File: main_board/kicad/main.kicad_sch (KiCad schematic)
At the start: 1 part

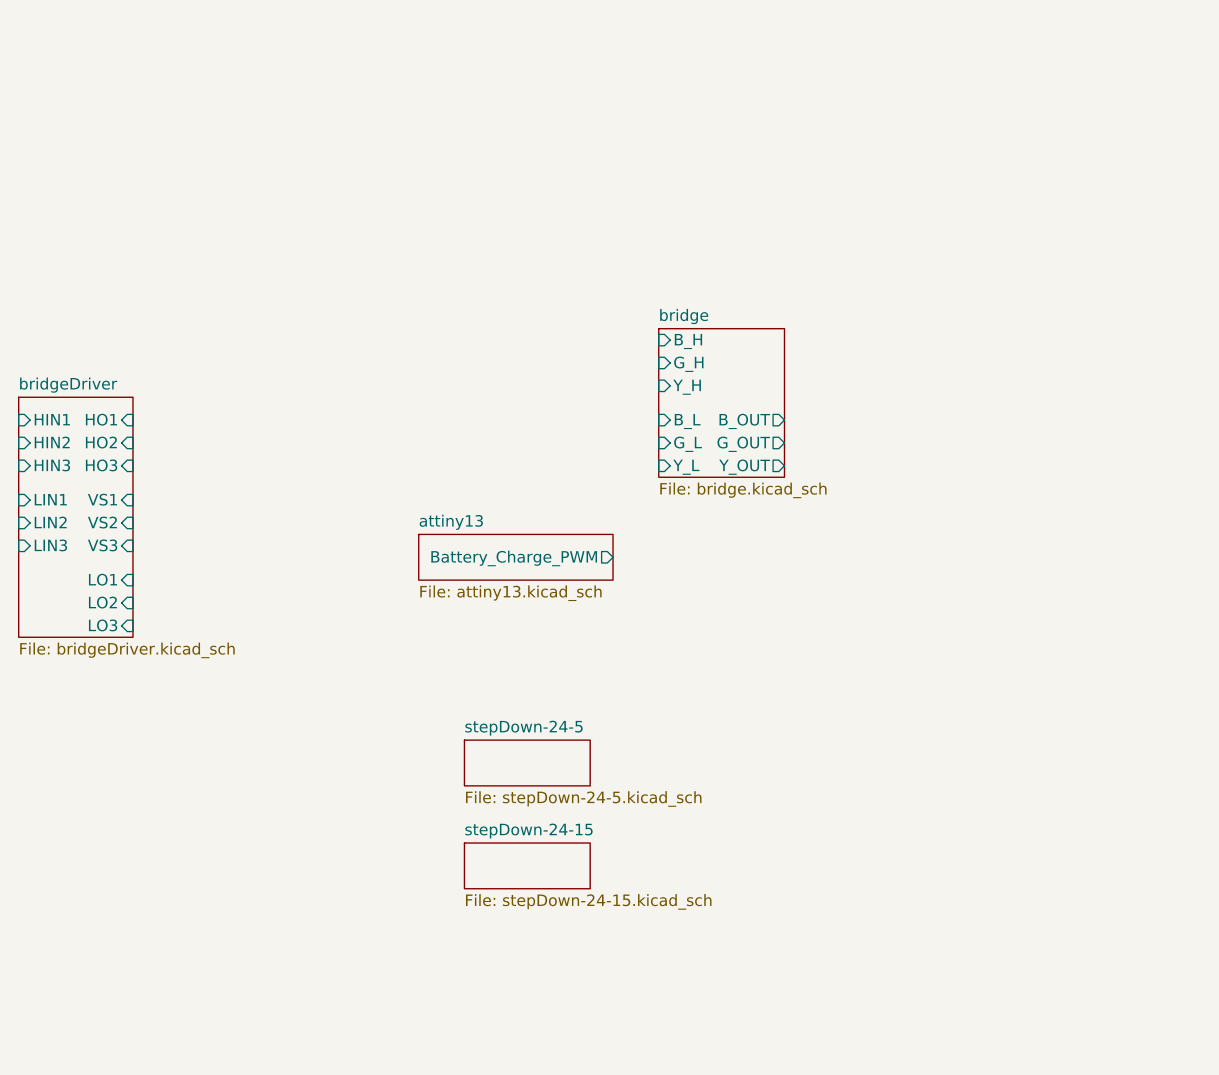
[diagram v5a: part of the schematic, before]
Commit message: added communication logic
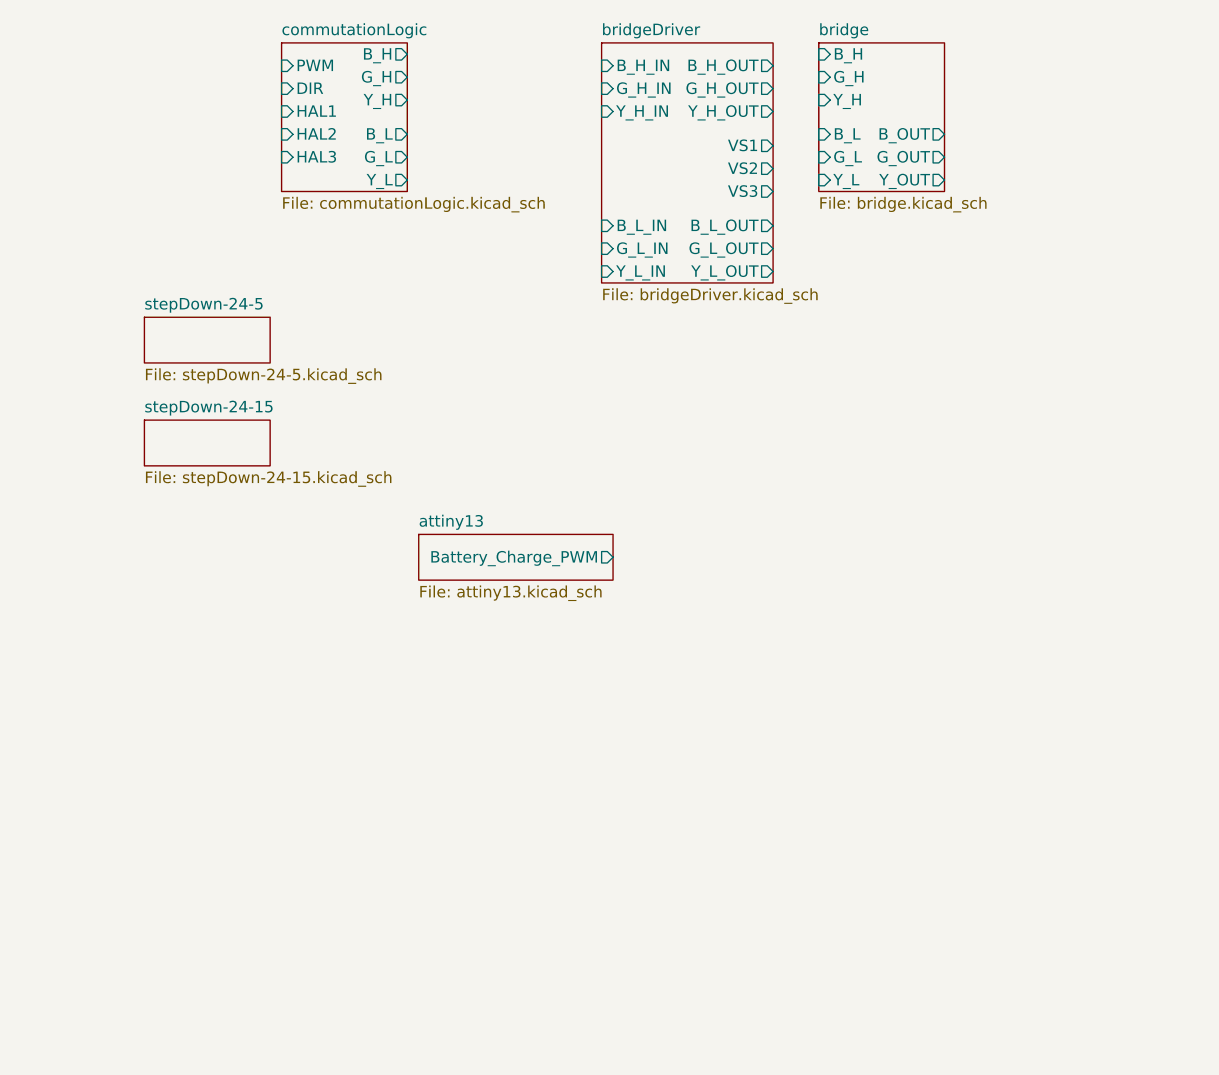
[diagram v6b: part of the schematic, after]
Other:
- added sheet commutationLogic (commutationLogic.kicad_sch)
- sheet bridgeDriver ports: added B_H_IN, B_H_OUT, B_L_IN, B_L_OUT, G_H_IN, G_H_OUT, G_L_IN, G_L_OUT, Y_H_IN, Y_H_OUT, Y_L_IN, Y_L_OUT; removed HIN1, HIN2, HIN3, HO1, HO2, HO3, LIN1, LIN2, LIN3, LO1, LO2, LO3
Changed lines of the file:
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@@
     )
   )
-  (sheet (at 180.34 138.43) (size 13.97 16.51) (fields_autoplaced)
+  (sheet (at 198.12 106.68) (size 13.97 16.51) (fields_autoplaced)
     (stroke (width 0.1524) (type solid))
     (fill (color 0 0 0 0.0000))
-    (property "Sheetname" "bridge" (at 180.34 137.7184 0)
+    (property "Sheetname" "bridge" (at 198.12 105.9684 0)
       (effects (font (size 1.27 1.27)) (justify left bottom))
     )
-    (property "Sheetfile" "bridge.kicad_sch" (at 180.34 155.5246 0)
+    (property "Sheetfile" "bridge.kicad_sch" (at 198.12 123.7746 0)
       (effects (font (size 1.27 1.27)) (justify left top))
     )
-    (pin "G_H" input (at 180.34 142.24 180)
+    (pin "G_H" input (at 198.12 110.49 180)
       (effects (font (size 1.27 1.27)) (justify left))
     )
-    (pin "Y_L" input (at 180.34 153.67 180)
+    (pin "Y_L" input (at 198.12 121.92 180)
       (effects (font (size 1.27 1.27)) (justify left))
     )
-    (pin "Y_OUT" output (at 194.31 153.67 0)
+    (pin "Y_OUT" output (at 212.09 121.92 0)
       (effects (font (size 1.27 1.27)) (justify right))
     )
-    (pin "Y_H" input (at 180.34 144.78 180)
+    (pin "Y_H" input (at 198.12 113.03 180)
       (effects (font (size 1.27 1.27)) (justify left))
     )
-    (pin "G_OUT" output (at 194.31 151.13 0)
+    (pin "G_OUT" output (at 212.09 119.38 0)
       (effects (font (size 1.27 1.27)) (justify right))
     )
-    (pin "G_L" input (at 180.34 151.13 180)
+    (pin "G_L" input (at 198.12 119.38 180)
       (effects (font (size 1.27 1.27)) (justify left))
     )
-    (pin "B_L" input (at 180.34 148.59 180)
+    (pin "B_L" input (at 198.12 116.84 180)
       (effects (font (size 1.27 1.27)) (justify left))
     )
-    (pin "B_OUT" output (at 194.31 148.59 0)
+    (pin "B_OUT" output (at 212.09 116.84 0)
       (effects (font (size 1.27 1.27)) (justify right))
     )
-    (pin "B_H" input (at 180.34 139.7 180)
+    (pin "B_H" input (at 198.12 107.95 180)
       (effects (font (size 1.27 1.27)) (justify left))
     )
@@
     )
   )
-  (sheet (at 158.75 195.58) (size 13.97 5.08) (fields_autoplaced)
+  (sheet (at 123.19 148.59) (size 13.97 5.08) (fields_autoplaced)
     (stroke (width 0.1524) (type solid))
     (fill (color 0 0 0 0.0000))
-    (property "Sheetname" "stepDown-24-15" (at 158.75 194.8684 0)
+    (property "Sheetname" "stepDown-24-15" (at 123.19 147.8784 0)
       (effects (font (size 1.27 1.27)) (justify left bottom))
     )
-    (property "Sheetfile" "stepDown-24-15.kicad_sch" (at 158.75 201.2446 0)
+    (property "Sheetfile" "stepDown-24-15.kicad_sch" (at 123.19 154.2546 0)
       (effects (font (size 1.27 1.27)) (justify left top))
     )
@@
     )
   )
-  (sheet (at 158.75 184.15) (size 13.97 5.08) (fields_autoplaced)
+  (sheet (at 123.19 137.16) (size 13.97 5.08) (fields_autoplaced)
     (stroke (width 0.1524) (type solid))
     (fill (color 0 0 0 0.0000))
-    (property "Sheetname" "stepDown-24-5" (at 158.75 183.4384 0)
+    (property "Sheetname" "stepDown-24-5" (at 123.19 136.4484 0)
       (effects (font (size 1.27 1.27)) (justify left bottom))
     )
-    (property "Sheetfile" "stepDown-24-5.kicad_sch" (at 158.75 189.8146 0)
+    (property "Sheetfile" "stepDown-24-5.kicad_sch" (at 123.19 142.8246 0)
       (effects (font (size 1.27 1.27)) (justify left top))
     )
@@
     )
   )
-  (sheet (at 109.22 146.05) (size 12.7 26.67) (fields_autoplaced)
+  (sheet (at 138.43 106.68) (size 13.97 16.51) (fields_autoplaced)
     (stroke (width 0.1524) (type solid))
     (fill (color 0 0 0 0.0000))
-    (property "Sheetname" "bridgeDriver" (at 109.22 145.3384 0)
+    (property "Sheetname" "commutationLogic" (at 138.43 105.9684 0)
       (effects (font (size 1.27 1.27)) (justify left bottom))
     )
-    (property "Sheetfile" "bridgeDriver.kicad_sch" (at 109.22 173.3046 0)
+    (property "Sheetfile" "commutationLogic.kicad_sch" (at 138.43 123.7746 0)
       (effects (font (size 1.27 1.27)) (justify left top))
     )
-    (pin "HIN1" input (at 109.22 148.59 180)
+    (pin "HAL2" input (at 138.43 116.84 180)
       (effects (font (size 1.27 1.27)) (justify left))
     )
-    (pin "HIN3" input (at 109.22 153.67 180)
+    (pin "HAL1" input (at 138.43 114.3 180)
       (effects (font (size 1.27 1.27)) (justify left))
     )
-    (pin "LIN1" input (at 109.22 157.48 180)
+    (pin "B_H" output (at 152.4 107.95 0)
+      (effects (font (size 1.27 1.27)) (justify right))
+    )
+    (pin "G_H" output (at 152.4 110.49 0)
+      (effects (font (size 1.27 1.27)) (justify right))
+    )
+    (pin "Y_H" output (at 152.4 113.03 0)
+      (effects (font (size 1.27 1.27)) (justify right))
+    )
+    (pin "B_L" output (at 152.4 116.84 0)
+      (effects (font (size 1.27 1.27)) (justify right))
+    )
+    (pin "G_L" output (at 152.4 119.38 0)
+      (effects (font (size 1.27 1.27)) (justify right))
+    )
+    (pin "Y_L" output (at 152.4 121.92 0)
+      (effects (font (size 1.27 1.27)) (justify right))
+    )
+    (pin "PWM" input (at 138.43 109.22 180)
       (effects (font (size 1.27 1.27)) (justify left))
     )
-    (pin "HIN2" input (at 109.22 151.13 180)
+    (pin "DIR" input (at 138.43 111.76 180)
       (effects (font (size 1.27 1.27)) (justify left))
     )
-    (pin "LIN2" input (at 109.22 160.02 180)
+    (pin "HAL3" input (at 138.43 119.38 180)
       (effects (font (size 1.27 1.27)) (justify left))
     )
-    (pin "LIN3" input (at 109.22 162.56 180)
+    (instances
+      (project "main"
+        (path "/9139d8e7-a5dc-421f-9a12-f77d83384a16" (page "7"))
+      )
+    )
+  )
+  (sheet (at 173.99 106.68) (size 19.05 26.67) (fields_autoplaced)
+    (stroke (width 0.1524) (type solid))
+    (fill (color 0 0 0 0.0000))
+    (property "Sheetname" "bridgeDriver" (at 173.99 105.9684 0)
+      (effects (font (size 1.27 1.27)) (justify left bottom))
+    )
+    (property "Sheetfile" "bridgeDriver.kicad_sch" (at 173.99 133.9346 0)
+      (effects (font (size 1.27 1.27)) (justify left top))
+    )
+    (pin "VS3" output (at 193.04 123.19 0)
+      (effects (font (size 1.27 1.27)) (justify right))
+    )
+    (pin "VS1" output (at 193.04 118.11 0)
+      (effects (font (size 1.27 1.27)) (justify right))
+    )
+    (pin "VS2" output (at 193.04 120.65 0)
+      (effects (font (size 1.27 1.27)) (justify right))
+    )
+    (pin "Y_L_IN" input (at 173.99 132.08 180)
       (effects (font (size 1.27 1.27)) (justify left))
     )
-    (pin "VS3" input (at 121.92 162.56 0)
+    (pin "G_H_IN" input (at 173.99 111.76 180)
+      (effects (font (size 1.27 1.27)) (justify left))
+    )
+    (pin "Y_H_IN" input (at 173.99 114.3 180)
+      (effects (font (size 1.27 1.27)) (justify left))
+    )
+    (pin "B_H_IN" input (at 173.99 109.22 180)
+      (effects (font (size 1.27 1.27)) (justify left))
+    )
+    (pin "B_L_IN" input (at 173.99 127 180)
+      (effects (font (size 1.27 1.27)) (justify left))
+    )
+    (pin "G_L_IN" input (at 173.99 129.54 180)
+      (effects (font (size 1.27 1.27)) (justify left))
+    )
+    (pin "G_L_OUT" output (at 193.04 129.54 0)
       (effects (font (size 1.27 1.27)) (justify right))
     )
-    (pin "LO1" input (at 121.92 166.37 0)
+    (pin "Y_L_OUT" output (at 193.04 132.08 0)
       (effects (font (size 1.27 1.27)) (justify right))
     )
-    (pin "LO3" input (at 121.92 171.45 0)
+    (pin "B_L_OUT" output (at 193.04 127 0)
       (effects (font (size 1.27 1.27)) (justify right))
     )
-    (pin "LO2" input (at 121.92 168.91 0)
+    (pin "Y_H_OUT" output (at 193.04 114.3 0)
       (effects (font (size 1.27 1.27)) (justify right))
     )
-    (pin "HO3" input (at 121.92 153.67 0)
+    (pin "G_H_OUT" output (at 193.04 111.76 0)
       (effects (font (size 1.27 1.27)) (justify right))
     )
-    (pin "VS1" input (at 121.92 157.48 0)
+    (pin "B_H_OUT" output (at 193.04 109.22 0)
       (effects (font (size 1.27 1.27)) (justify right))
     )
-    (pin "VS2" input (at 121.92 160.02 0)
-      (effects (font (size 1.27 1.27)) (justify right))
-    )
-    (pin "HO2" input (at 121.92 151.13 0)
-      (effects (font (size 1.27 1.27)) (justify right))
-    )
-    (pin "HO1" input (at 121.92 148.59 0)
-      (effects (font (size 1.27 1.27)) (justify right))
-    )

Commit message: huh
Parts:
- added J2, J3: Motorbuchse, 2022-lsd:Motorbuchse, symbol 2022-lsd:Motorbuchse
- added J4: Batteriebuchse, 2022-lsd:Batteriebuchse, symbol 2022-lsd:Batteriebuchse
- added J5: Conn_02x07_Odd_Even, symbol Connector_Generic:Conn_02x07_Odd_Even
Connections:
- net bridge/B_OUT: now also J2.1
- net bridge/G_OUT: now also J2.2
- net bridge/Y_OUT: now also J2.3
- new net +24V: J4.2 (VBAT), J4.3 (VBAT)
- new net +5V: J5.12 (Pin_12), J5.13 (Pin_13), J5.14 (Pin_14)
- new net BAT_CHARGE_PWM: J5.7 (Pin_7)
- new net DIR_L_REG: J5.3 (Pin_3)
- new net DIR_R_REG: J5.4 (Pin_4)
- new net ENABLE_L_REG: J5.5 (Pin_5)
- new net ENABLE_R_REG: J5.6 (Pin_6)
- new net GND: J4.1 (GND), J4.4 (GND), J5.10 (Pin_10), J5.11 (Pin_11), J5.8 (Pin_8), J5.9 (Pin_9)
- new net PWM_L_REG: J5.1 (Pin_1)
- new net PWM_R_REG: J5.2 (Pin_2)
- new net bridge1/B_OUT: J3.1
- new net bridge1/G_OUT: J3.2
- new net bridge1/Y_OUT: J3.3
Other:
- added sheet bridge1 (bridge.kicad_sch)
- added sheet bridgeDriver1 (bridgeDriver.kicad_sch)
- added sheet commutationLogic1 (commutationLogic.kicad_sch)
